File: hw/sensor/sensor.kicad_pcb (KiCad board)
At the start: 2 copper layers, 33.5 x 60 mm, 17 parts, among them J1 Screw_Terminal_01x02, J2 Conn_ST_STDC14, U1 STM32G031K8Tx, U2 RFM69HW, Y1 32.768KHz

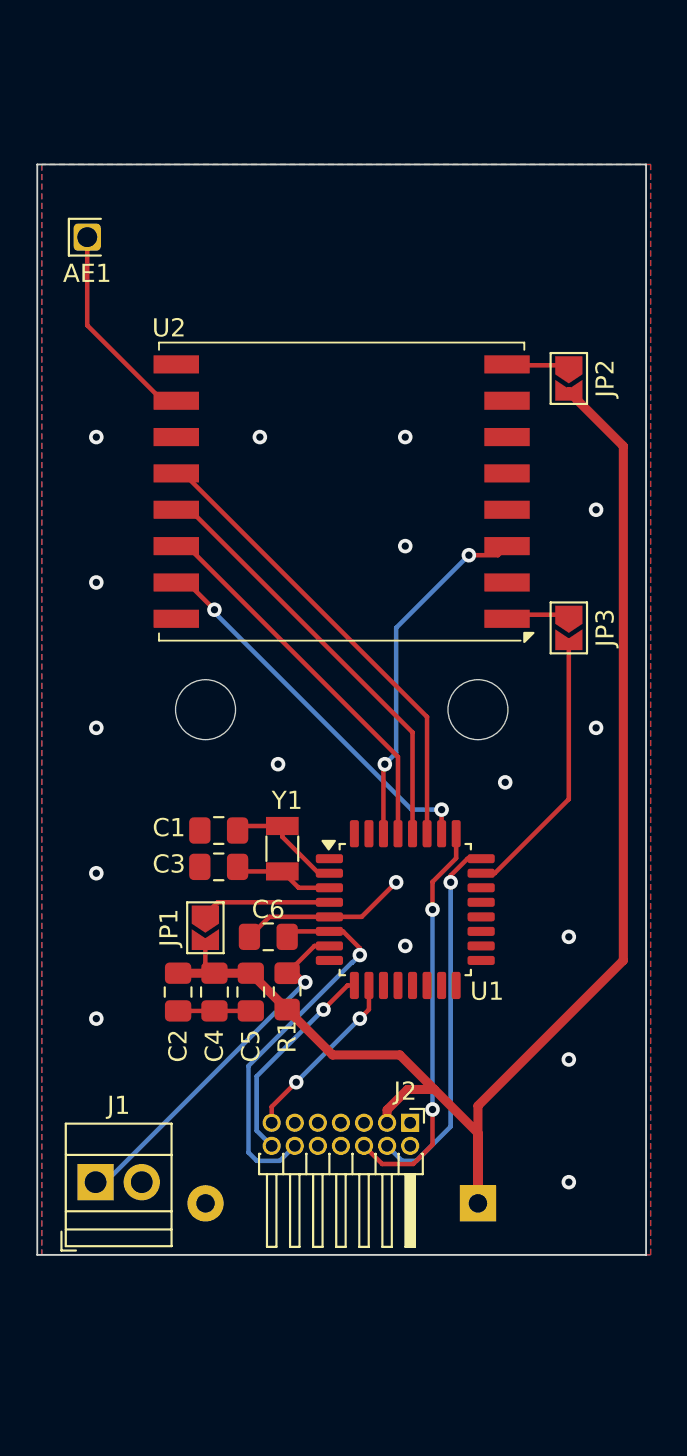
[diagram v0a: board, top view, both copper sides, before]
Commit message: sensor redesigned
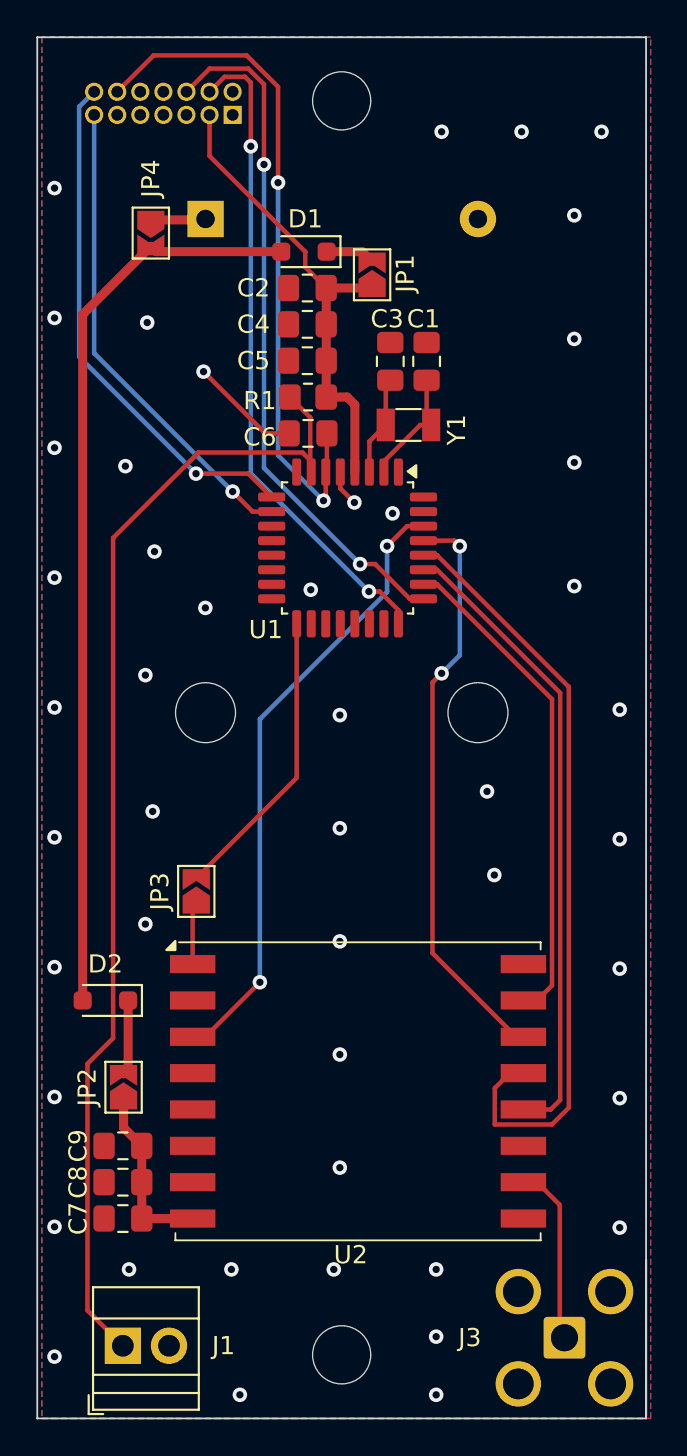
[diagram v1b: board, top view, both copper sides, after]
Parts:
- removed AE1: Antenna, RF_Antenna:NiceRF_SW868-TH13_868Mhz
- added C7: 4.7uF, Capacitor_SMD:C_0805_2012Metric_Pad1.18x1.45mm_HandSolder, F.Cu at (113.5, 90.5)
- added C8: 100nF, Capacitor_SMD:C_0805_2012Metric_Pad1.18x1.45mm_HandSolder, F.Cu at (113.5, 88.5)
- added C9: 100nF, Capacitor_SMD:C_0805_2012Metric_Pad1.18x1.45mm_HandSolder, F.Cu at (113.5, 86.5)
- added D1: D_Schottky, Diode_SMD:D_SOD-323_HandSoldering, F.Cu at (123.4, 37.3)
- added D2: D_Schottky, Diode_SMD:D_SOD-323_HandSoldering, F.Cu at (112.5, 78.5)
- added H1: MountingHole, MountingHole:MountingHole_3.2mm_M3, F.Cu at (125.5, 29.0)
- added H4: MountingHole, MountingHole:MountingHole_3.2mm_M3, F.Cu at (125.5, 98.0)
- added J3: Conn_Coaxial, Connector_Coaxial:SMA_Amphenol_901-143_Horizontal, B.Cu at (137.8, 97.1)
- added JP4: SolderJumper_2_Bridged, Jumper:SolderJumper-2_P1.3mm_Open_TrianglePad1.0x1.5mm, F.Cu at (115.0, 36.3)
- J2: footprint Connector_PinHeader_1.27mm:PinHeader_2x07_P1.27mm_Horizontal -> Connector_PinHeader_1.27mm:PinHeader_2x07_P1.27mm_Vertical; moved to B.Cu
- moved J2 56.3 mm to (119.5, 29.8), turned to 90 degrees
- moved BT1 56.2 mm to (118.0, 35.5), turned to -90 degrees
- moved JP2 46.1 mm to (113.5, 83.3), turned to 90 degrees
- moved C2 39.4 mm to (123.6, 39.3), turned to 180 degrees
- moved C4 37.1 mm to (123.6, 41.3), turned to 180 degrees
- moved JP1 37.1 mm to (127.2, 38.6), turned to 90 degrees
- moved C5 34.9 mm to (123.6, 43.3), turned to 180 degrees
- moved U2 33.0 mm to (126.4, 83.5), turned to 0 degrees
- moved R1 32.7 mm to (123.7, 45.3), turned to 180 degrees
- moved C3 29.4 mm to (128.2, 43.3), turned to 90 degrees
- moved C1 28.2 mm to (130.2, 43.3), turned to 90 degrees
- moved C6 27.8 mm to (123.7, 47.3)
- moved JP3 25.1 mm to (117.5, 72.5), turned to 90 degrees
- moved Y1 24.3 mm to (129.2, 46.8), turned to 0 degrees
- moved U1 20.2 mm to (125.8, 53.6), turned to -90 degrees
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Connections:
- net Net-(JP2-A) renamed RFM_3v3
- BT1 pad 1: +BATT -> Net-(BT1-+)
- C2 pad 1: +BATT -> STM_3v3
- C4 pad 1: +BATT -> STM_3v3
- C5 pad 1: +BATT -> STM_3v3
- J2 pad 3: +BATT -> STM_3v3
- JP1 pad 1: Net-(JP1-A) -> STM_3v3
- JP1 pad 2: +BATT -> Net-(D1-K)
- JP2 pad 2: +BATT -> Net-(D2-K)
- R1 pad 1: +BATT -> STM_3v3
- U1 pad 17: unconnected-(U1-PB2-Pad17) -> /RFM_RESET
- U1 pad 23: /RFM_RESET -> unconnected-(U1-PA12/PA10-Pad23)
- U1 pad 4: Net-(JP1-A) -> STM_3v3
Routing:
- net +BATT: track 79.0 -> 0.00 mm
- net Net-(D1-A): track 0.00 -> 50.3 mm
- net Net-(J1-Pin_1): track 20.2 -> 64.1 mm, vias 1 -> 0
- net STM_3v3: track 0.00 -> 26.2 mm
- net /RFM_MISO: track 23.6 -> 42.5 mm
- net /UART_TX: track 11.6 -> 28.7 mm
- net /UART_RX: track 9.77 -> 26.5 mm, vias 2 -> 1
- net /RST: track 21.4 -> 38.0 mm, vias 1 -> 2
- net /SWDIO: track 20.5 -> 36.2 mm, vias 1 -> 2
- net /SWCLK: track 22.3 -> 38.0 mm
- net /RFM_IRQ: track 19.6 -> 34.3 mm
- net /RFM_MOSI: track 21.2 -> 32.1 mm, vias 0 -> 2
- net /RFM_SCK: track 25.8 -> 35.0 mm
- net Net-(JP1-A): track 7.10 -> 0.00 mm
- net RFM_3v3: track 3.42 -> 9.71 mm
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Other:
- board size 33.5 x 60 mm -> 33.5 x 76 mm
- board text added: "Win sensor v1"
